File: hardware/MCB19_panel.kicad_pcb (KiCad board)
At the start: 2 copper layers, 204 x 171.5 mm, 218 parts, among them J401 USART, J402 DISABLE, J601 RJ45, J602 RJ45, J611 +BAT_IN, J612 -BAT_IN, J613 +BAT_OUT, J614 -BAT_OUT, Q601 IRFP260N, Q602 IRFP260N, U201 MCP2551-I/SN, U202 MCP2515-xSO, U301 LM7805, U401 ATMEGA328P-PU, U501 LM7815, U601 LM5104MNOPB, U602 INA240A4D, U603 LM324, Y201 16MHz, Y401 16MHz

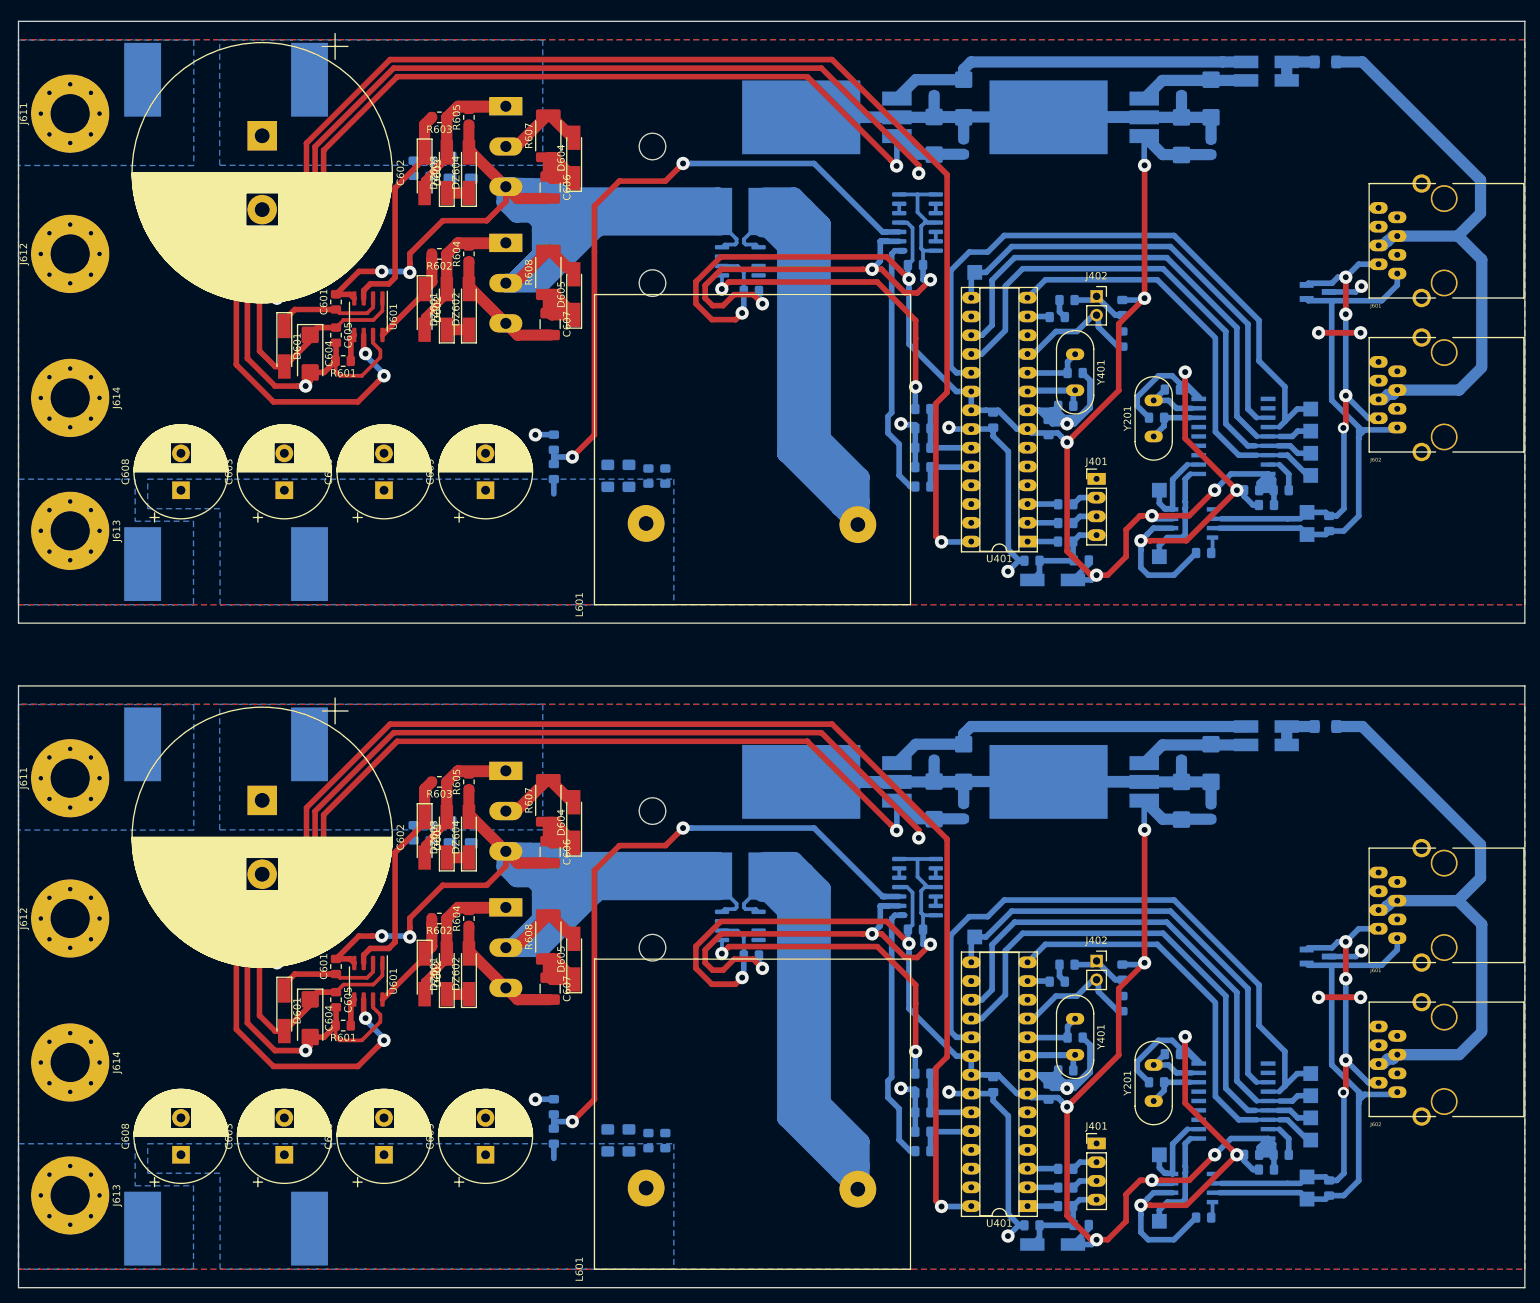
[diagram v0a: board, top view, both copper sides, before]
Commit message: small fixes in layout. Fabrication files exported.
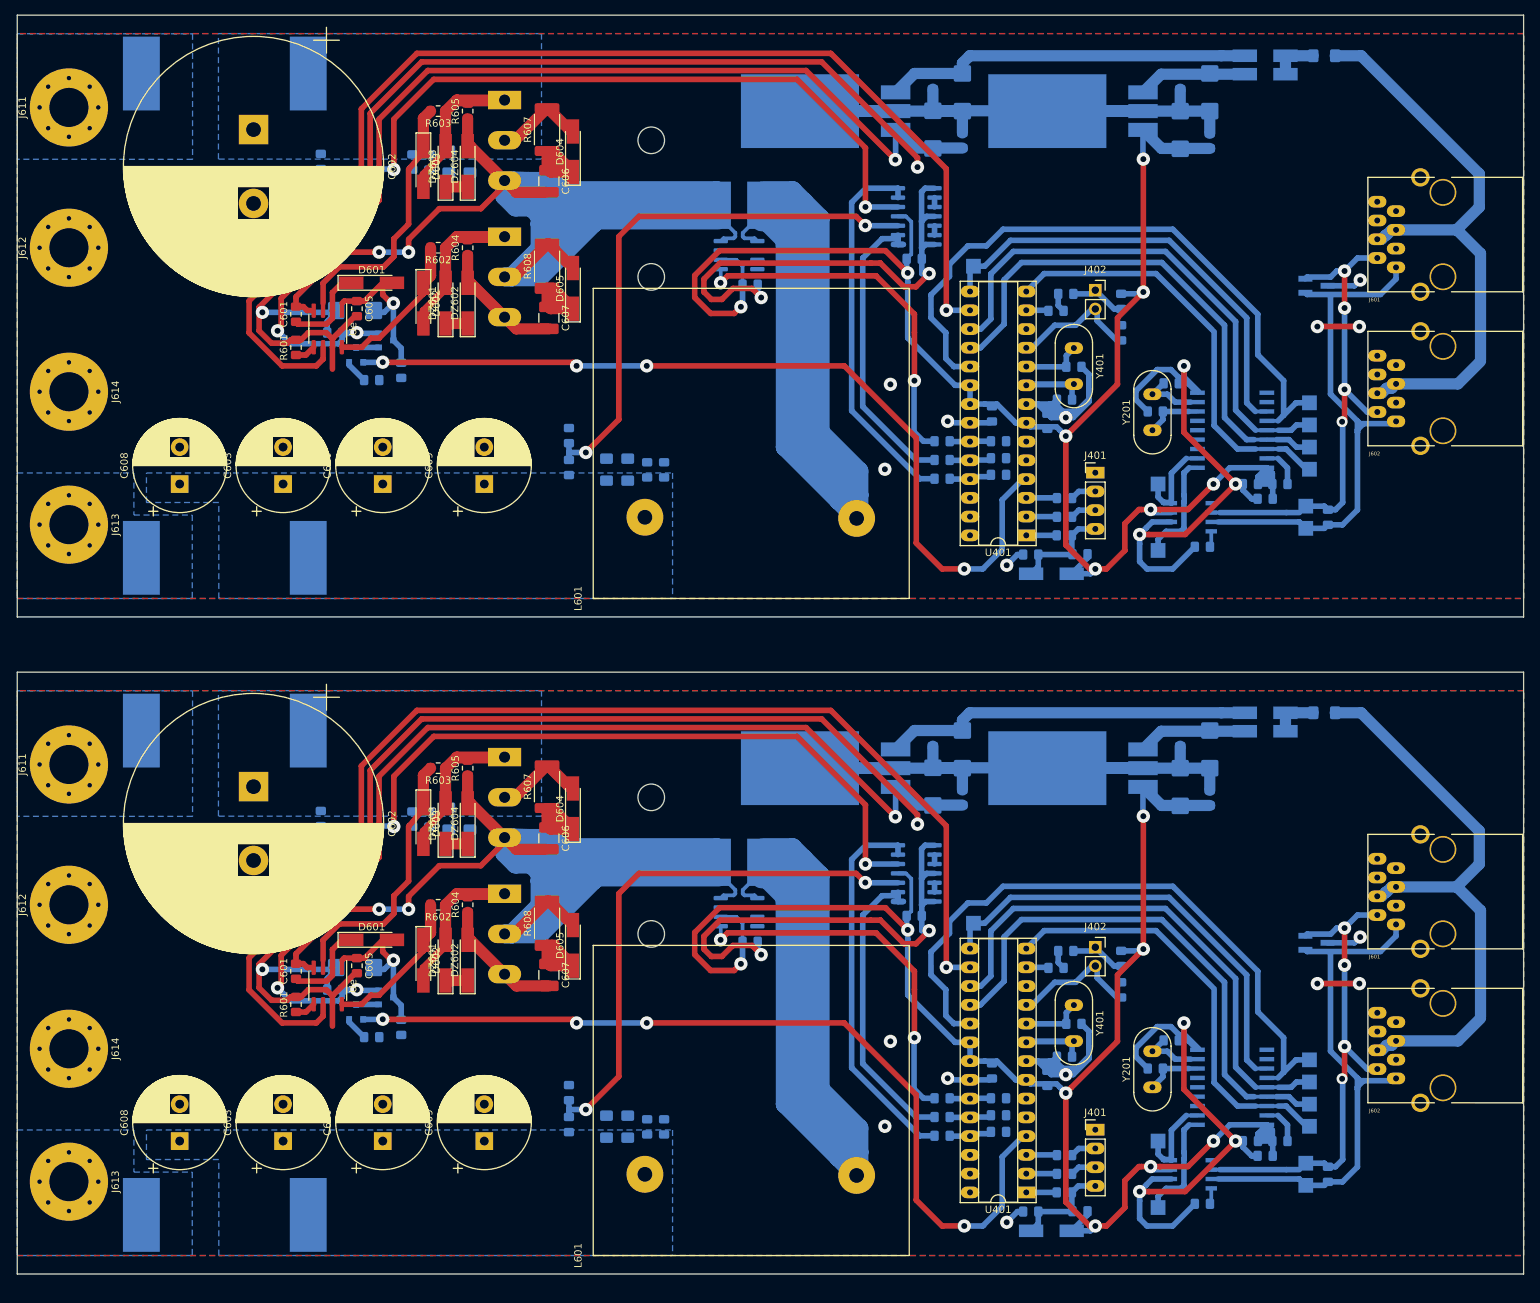
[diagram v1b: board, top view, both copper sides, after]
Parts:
- removed the D601 at (83.6, 154.9)
- removed the D601 at (83.6, 64.9)
- removed U601: LM5104MNOPB, Package_SO:SOIC-8_3.9x4.9mm_P1.27mm
- added C409: 100nF, Capacitor_SMD:C_0805_2012Metric_Pad1.15x1.40mm_HandSolder, B.Cu at (180.3, 171.2)
- added C409: 100nF, Capacitor_SMD:C_0805_2012Metric_Pad1.15x1.40mm_HandSolder, B.Cu at (180.3, 82.3)
- added C621: 100nF, Capacitor_SMD:C_0805_2012Metric_Pad1.15x1.40mm_HandSolder, B.Cu at (90.5, 152.0)
- added C621: 100nF, Capacitor_SMD:C_0805_2012Metric_Pad1.15x1.40mm_HandSolder, B.Cu at (90.5, 63.0)
- added D601: LL4148, Diode_SMD:D_MiniMELF_Handsoldering, F.Cu at (95.5, 145.2)
- added D601: LL4148, Diode_SMD:D_MiniMELF_Handsoldering, F.Cu at (95.5, 56.3)
- added Q603: BC857, Package_TO_SOT_SMD:SOT-23, B.Cu at (97.4, 153.0)
- added Q603: BC857, Package_TO_SOT_SMD:SOT-23, B.Cu at (97.4, 64.1)
- added Q604: BC847, Package_TO_SOT_SMD:SOT-23, B.Cu at (93.4, 155.0)
- added Q604: BC847, Package_TO_SOT_SMD:SOT-23, B.Cu at (93.4, 66.0)
- added R611: 1k, Resistor_SMD:R_0805_2012Metric_Pad1.15x1.40mm_HandSolder, B.Cu at (95.5, 158.4)
- added R611: 1k, Resistor_SMD:R_0805_2012Metric_Pad1.15x1.40mm_HandSolder, B.Cu at (95.5, 69.4)
- added R612: 1k, Resistor_SMD:R_0805_2012Metric_Pad1.15x1.40mm_HandSolder, B.Cu at (99.5, 157.1)
- added R612: 1k, Resistor_SMD:R_0805_2012Metric_Pad1.15x1.40mm_HandSolder, B.Cu at (99.5, 68.1)
- added R613: 15k, Resistor_SMD:R_0805_2012Metric_Pad1.15x1.40mm_HandSolder, B.Cu at (88.6, 128.8)
- added R613: 15k, Resistor_SMD:R_0805_2012Metric_Pad1.15x1.40mm_HandSolder, B.Cu at (88.6, 39.8)
- added R614: 1k2, Resistor_SMD:R_0805_2012Metric_Pad1.15x1.40mm_HandSolder, B.Cu at (88.6, 133.1)
- added R614: 1k2, Resistor_SMD:R_0805_2012Metric_Pad1.15x1.40mm_HandSolder, B.Cu at (88.6, 44.2)
- added Ue: LM5104MNOPB, Package_SO:SOIC-8_3.9x4.9mm_P1.27mm, F.Cu at (89.5, 151.5)
- C407 (x2): value 100n -> 100nF
- C604 (x2): moved to B.Cu
- R407 (x2), R408 (x2): value 1k5 -> 680
- R409 (x2): value 6k8 -> 680
- R609 (x2): value 470R -> 15k
- R610 (x2): value 1k5 -> 1k2
- moved C408 10.5 mm to (180.3, 169.0), turned to 0 degrees
- moved C407 10.4 mm to (180.3, 166.7), turned to 180 degrees
- moved C408 10.3 mm to (180.3, 80.0), turned to 0 degrees
- moved C407 10.3 mm to (180.3, 77.7), turned to 180 degrees
- moved C604 9.17 mm to (93.2, 149.0), turned to 180 degrees
- moved C604 8.43 mm to (93.2, 60.0), turned to 180 degrees
- moved R409 7.30 mm to (172.7, 82.8), turned to 180 degrees
- moved R601 7.01 mm to (85.2, 154.0), turned to 90 degrees
- moved R601 6.65 mm to (85.2, 65.0), turned to 90 degrees
- moved R409 6.36 mm to (172.7, 171.8), turned to 180 degrees
- moved R610 6.24 mm to (122.2, 165.9), turned to 270 degrees
- moved Ue 5.75 mm to (89.5, 62.5)
- moved C601 5.67 mm to (85.2, 60.5)
- moved C601 5.46 mm to (85.2, 149.5)
- moved C605 5.41 mm to (93.5, 148.8)
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- renumbered U601 to Ue
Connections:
- C604 pad 1: +15V -> Net-(C604-Pad1)
- C605 pad 1: +15V -> Net-(C604-Pad1)
- J601 pad 9: GND -> (no net)
- J602 pad 9: GND -> (no net)
- R409 pad 1: GND -> Net-(C409-Pad1)
- R409 pad 2: Net-(C407-Pad2) -> /driver/LM324B
- R609 pad 1: GND -> Net-(R609-Pad1)
- R609 pad 2: Net-(R609-Pad2) -> Net-(C603-Pad1)
- R610 pad 1: Net-(C603-Pad1) -> GND
- R610 pad 2: Net-(R609-Pad2) -> Net-(R609-Pad1)
- U401 pad 16: (no net) -> /MCU/PWM
- U401 pad 25: (no net) -> Net-(C409-Pad1)
- U401 pad 28: /MCU/PWM -> (no net)
- U401 pad 4: (no net) -> /MCU/ENABLE
- U603 pad 2: GND -> /driver/LM324A
- U603 pad 3: Net-(R609-Pad2) -> Net-(R609-Pad1)
- U603 pad 5: Net-(U603-Pad5) -> Net-(R613-Pad1)
- U603 pad 6: Net-(U603-Pad5) -> /driver/LM324B
- U603 pad 7: GND -> /driver/LM324B
- Ue pad 1: +15V -> Net-(C604-Pad1)
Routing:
- net (no net): track 2789.2 -> 2989.4 mm, vias 39 -> 44
- net /MCU/ENABLE: track 0.00 -> 119.1 mm, vias 0 -> 4
- net Net-(R613-Pad1): track 0.00 -> 101.3 mm, vias 0 -> 2
- net Net-(R609-Pad2): track 89.4 -> 0.00 mm, vias 2 -> 0
- net Net-(R609-Pad1): track 0.00 -> 75.1 mm, vias 0 -> 2
- net /MCU/PWM: track 217.1 -> 161.7 mm, vias 3 -> 1
- net /driver/LM324B: track 0.00 -> 51.6 mm
- net GND: track 558.8 -> 512.2 mm, vias 17 -> 15
- net Net-(C604-Pad1): track 0.00 -> 22.9 mm, vias 0 -> 1
- net +15V: track 158.4 -> 148.0 mm, vias 1 -> 3
- net /MCU/INALLL: track 42.7 -> 49.9 mm
- net Net-(D602-Pad1): track 13.7 -> 20.7 mm
- net Net-(D603-Pad1): track 30.3 -> 37.0 mm
- net Net-(C601-Pad2): track 253.7 -> 259.8 mm
- net Net-(Q603-Pad1): track 0.00 -> 6.12 mm
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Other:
- board size 204 x 171.5 mm -> 204 x 170.5 mm

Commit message: Some fixes, ready for heat transfering
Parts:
- removed the C201 at (197.0, 147.8)
- removed the C201 at (197.0, 58.8)
- removed the C202 at (214.5, 172.5)
- removed the C202 at (214.5, 83.5)
- removed the C203 at (201.6, 162.7)
- removed the C203 at (201.6, 73.7)
- removed the C204 at (203.7, 158.9)
- removed the C204 at (203.7, 69.9)
- removed the C205 at (216.5, 174.5)
- removed the C205 at (216.5, 85.5)
- removed the C301 at (209.0, 119.5)
- removed the C301 at (209.0, 30.5)
- removed the C302 at (205.0, 118.0)
- removed the C302 at (205.0, 29.0)
- removed the C303 at (209.0, 126.0)
- removed the C303 at (209.0, 37.0)
- removed the C304 at (205.0, 124.5)
- removed the C304 at (205.0, 35.6)
- removed the C401 at (187.0, 164.0)
- removed the C401 at (187.0, 75.0)
- removed the C402 at (179.5, 163.0)
- removed the C402 at (179.5, 74.0)
- removed the C403 at (190.6, 156.6)
- removed the C403 at (190.6, 67.6)
- removed the C404 at (189.3, 161.1)
- removed the C404 at (189.3, 72.1)
- removed the C406 at (184.7, 182.1)
- removed the C406 at (184.7, 93.1)
- removed the C407 at (180.3, 166.7)
- removed the C407 at (180.3, 77.7)
- removed the C408 at (180.3, 169.0)
- removed the C408 at (180.3, 80.0)
- removed the C409 at (180.3, 171.2)
- removed the C409 at (180.3, 82.3)
- removed the C501 at (175.5, 119.5)
- removed the C501 at (175.5, 30.5)
- removed the C502 at (171.5, 118.0)
- removed the C502 at (171.5, 29.0)
- removed the C503 at (175.5, 126.0)
- removed the C503 at (175.5, 37.0)
- removed the C504 at (171.5, 124.5)
- removed the C504 at (171.5, 35.5)
- removed the C601 at (85.2, 149.5)
- removed the C601 at (85.2, 60.5)
- removed the C602 at (79.5, 124.5)
- removed the C602 at (79.5, 35.5)
- removed the C603 at (83.5, 172.5)
- removed the C603 at (83.5, 83.5)
- removed the C604 at (93.2, 149.0)
- removed the C604 at (93.2, 60.0)
- removed the C605 at (93.5, 148.8)
- removed the C605 at (93.5, 59.8)
- removed the C606 at (119.5, 131.5)
- removed the C606 at (119.5, 42.5)
- removed the C607 at (119.5, 150.0)
- removed the C607 at (119.5, 61.0)
- removed the C608 at (69.5, 172.5)
- removed the C608 at (69.5, 83.5)
- removed the C609 at (110.7, 172.5)
- removed the C609 at (110.7, 83.5)
- removed the C610 at (97.0, 172.5)
- removed the C610 at (97.0, 83.5)
- removed the C611 at (146.7, 145.5)
- removed the C611 at (146.7, 56.5)
- removed the C612 at (168.9, 142.0)
- removed the C612 at (168.9, 53.0)
- removed the C613 at (108.8, 128.8)
- removed the C613 at (108.8, 39.9)
- removed the C614 at (105.9, 128.8)
- removed the C614 at (105.9, 39.9)
- removed the C615 at (101.0, 128.9)
- removed the C615 at (101.0, 39.9)
- removed the C616 at (103.3, 128.9)
- removed the C616 at (103.3, 39.9)
- removed the C617 at (130.1, 170.6)
- removed the C617 at (130.1, 81.6)
- removed the C618 at (127.3, 170.6)
- removed the C618 at (127.3, 81.6)
- removed the C619 at (135.1, 170.6)
- removed the C619 at (135.1, 81.6)
- removed the C620 at (132.8, 170.6)
- removed the C620 at (132.8, 81.6)
- removed the C621 at (90.5, 152.0)
- removed the C621 at (90.5, 63.0)
- removed the D201 at (223.4, 145.7)
- removed the D201 at (223.4, 56.7)
- removed the D301 at (216.5, 117.0)
- removed the D301 at (216.5, 28.0)
- removed the D401 at (187.5, 184.7)
- removed the D401 at (187.5, 95.7)
- removed the D403 at (189.5, 146.8)
- removed the D403 at (189.5, 57.8)
- removed the D501 at (216.5, 114.5)
- removed the D501 at (216.5, 25.5)
- removed the D601 at (95.5, 145.2)
- removed the D601 at (95.5, 56.3)
- removed the D602 at (102.5, 148.0)
- removed the D602 at (102.5, 59.0)
- removed the D603 at (102.5, 129.5)
- removed the D603 at (102.5, 40.5)
- removed the D604 at (122.7, 127.5)
- removed the D604 at (122.7, 38.5)
- removed the D605 at (122.7, 146.0)
- removed the D605 at (122.7, 57.0)
- removed the DZ601 at (105.5, 148.0)
- removed the DZ601 at (105.5, 59.0)
- removed the DZ602 at (108.5, 148.0)
- removed the DZ602 at (108.5, 59.0)
- removed the DZ603 at (105.5, 129.5)
- removed the DZ603 at (105.5, 40.5)
- removed the DZ604 at (108.5, 129.5)
- removed the DZ604 at (108.5, 40.5)
- removed the F501 at (224.5, 114.5)
- removed the F501 at (224.5, 25.5)
- removed the F601 at (86.9, 116.9)
- removed the F601 at (86.9, 27.9)
- removed the F602 at (64.3, 182.5)
- removed the F602 at (64.3, 93.5)
- removed the J401 at (193.5, 171.0)
- removed the J401 at (193.5, 82.0)
- removed the J402 at (193.5, 146.2)
- removed the J402 at (193.5, 57.3)
- removed the J601 at (234.2, 143.2)
- removed the J601 at (234.2, 54.2)
- removed the J602 at (234.2, 164.0)
- removed the J602 at (234.2, 75.0)
- removed the J611 at (54.5, 121.5)
- removed the J611 at (54.5, 32.5)
- removed the J612 at (54.5, 140.5)
- removed the J612 at (54.5, 51.5)
- removed the J613 at (54.5, 178.0)
- removed the J613 at (54.5, 89.0)
- removed the J614 at (54.5, 160.0)
- removed the J614 at (54.5, 71.0)
- removed the L601 at (125.5, 188.0)
- removed the L601 at (125.5, 99.0)
- removed the Q601 at (113.5, 120.5)
- removed the Q601 at (113.5, 31.5)
- removed the Q602 at (113.5, 139.0)
- removed the Q602 at (113.5, 50.0)
- removed the Q603 at (97.4, 153.0)
- removed the Q603 at (97.4, 64.1)
- removed the Q604 at (93.4, 155.0)
- removed the Q604 at (93.4, 66.0)
- removed the R201 at (225.0, 177.0)
- removed the R201 at (225.0, 88.0)
- removed the R202 at (208.0, 181.0)
- removed the R202 at (208.0, 92.0)
- removed the R203 at (218.5, 172.5)
- removed the R203 at (218.5, 83.5)
- removed the R401 at (191.4, 182.0)
- removed the R401 at (191.4, 93.0)
- removed the R402 at (189.3, 176.9)
- removed the R402 at (189.3, 88.0)
- removed the R403 at (189.3, 174.4)
- removed the R403 at (189.3, 85.4)
- removed the R406 at (188.1, 149.1)
- removed the R406 at (188.1, 60.1)
- removed the R407 at (172.7, 166.7)
- removed the R407 at (172.7, 77.7)
- removed the R408 at (172.7, 169.2)
- removed the R408 at (172.7, 80.3)
- removed the R409 at (172.7, 171.8)
- removed the R409 at (172.7, 82.8)
- removed the R410 at (197.0, 152.0)
- removed the R410 at (197.0, 63.0)
- removed the R411 at (189.3, 179.4)
- removed the R411 at (189.3, 90.5)
- removed the R601 at (85.2, 154.0)
- removed the R601 at (85.2, 65.0)
- removed the R602 at (104.5, 140.5)
- removed the R602 at (104.5, 51.5)
- removed the R603 at (104.5, 122.0)
- removed the R603 at (104.5, 33.0)
- removed the R604 at (108.5, 140.5)
- removed the R604 at (108.5, 51.5)
- removed the R605 at (108.5, 122.0)
- removed the R605 at (108.5, 33.0)
- removed the R606 at (145.2, 134.8)
- removed the R606 at (145.2, 45.8)
- removed the R607 at (119.2, 124.5)
- removed the R607 at (119.2, 35.5)
- removed the R608 at (119.2, 143.0)
- removed the R608 at (119.2, 54.0)
- removed the R609 at (122.2, 170.3)
- removed the R609 at (122.2, 81.3)
- removed the R610 at (122.2, 165.9)
- removed the R610 at (122.2, 77.0)
- removed the R611 at (95.5, 158.4)
- removed the R611 at (95.5, 69.4)
- removed the R612 at (99.5, 157.1)
- removed the R612 at (99.5, 68.1)
- removed the R613 at (88.6, 128.8)
- removed the R613 at (88.6, 39.8)
- removed the R614 at (88.6, 133.1)
- removed the R614 at (88.6, 44.2)
- removed the TP201 at (222.5, 164.5)
- removed the TP201 at (222.5, 75.5)
- removed the TP202 at (222.5, 167.5)
- removed the TP202 at (222.5, 78.5)
- removed the TP203 at (202.0, 181.5)
- removed the TP203 at (202.0, 92.5)
- removed the TP204 at (202.0, 172.5)
- removed the TP204 at (202.0, 83.5)
- removed the TP205 at (222.5, 170.5)
- removed the TP205 at (222.5, 81.5)
- removed the TP206 at (222.5, 161.5)
- removed the TP206 at (222.5, 72.5)
- removed the TP207 at (222.0, 178.5)
- removed the TP207 at (222.0, 89.5)
- removed the TP208 at (222.0, 175.5)
- removed the TP208 at (222.0, 86.5)
- removed the TP209 at (177.0, 143.0)
- removed the TP209 at (177.0, 54.0)
- removed the U201 at (206.5, 177.0)
- removed the U201 at (206.5, 88.0)
- removed the U202 at (212.0, 165.2)
- removed the U202 at (212.0, 76.2)
- removed the U301 at (198.6, 119.5)
- removed the U301 at (198.6, 30.5)
- removed the U401 at (184.1, 179.4)
- removed the U401 at (184.1, 90.5)
- removed the U501 at (165.1, 119.5)
- removed the U501 at (165.1, 30.5)
- removed the U602 at (145.2, 141.5)
- removed the U602 at (145.2, 52.5)
- removed the U603 at (169.2, 136.2)
- removed the U603 at (169.2, 47.3)
- removed Ue (x2): LM5104MNOPB, Package_SO:SOIC-8_3.9x4.9mm_P1.27mm
- removed the Y201 at (201.2, 165.2)
- removed the Y201 at (201.2, 76.2)
- removed the Y401 at (190.6, 154.1)
- removed the Y401 at (190.6, 65.1)
- added C201: 100nF, Capacitor_SMD:C_0805_2012Metric_Pad1.15x1.40mm_HandSolder, B.Cu at (236.5, 69.1)
- added C201: 100nF, Capacitor_SMD:C_0805_2012Metric_Pad1.15x1.40mm_HandSolder, B.Cu at (146.5, 69.1)
- added C201: 100nF, Capacitor_SMD:C_0805_2012Metric_Pad1.15x1.40mm_HandSolder, B.Cu at (56.5, 69.1)
- added C202: 100nF, Capacitor_SMD:C_0805_2012Metric_Pad1.15x1.40mm_HandSolder, B.Cu at (261.2, 51.6)
- added C202: 100nF, Capacitor_SMD:C_0805_2012Metric_Pad1.15x1.40mm_HandSolder, B.Cu at (171.2, 51.6)
- added C202: 100nF, Capacitor_SMD:C_0805_2012Metric_Pad1.15x1.40mm_HandSolder, B.Cu at (81.2, 51.6)
- added C203: 22pF, Capacitor_SMD:C_0805_2012Metric_Pad1.15x1.40mm_HandSolder, B.Cu at (251.4, 64.5)
- added C203: 22pF, Capacitor_SMD:C_0805_2012Metric_Pad1.15x1.40mm_HandSolder, B.Cu at (161.4, 64.5)
- added C203: 22pF, Capacitor_SMD:C_0805_2012Metric_Pad1.15x1.40mm_HandSolder, B.Cu at (71.4, 64.5)
- added C204: 22pF, Capacitor_SMD:C_0805_2012Metric_Pad1.15x1.40mm_HandSolder, B.Cu at (247.6, 62.3)
- added C204: 22pF, Capacitor_SMD:C_0805_2012Metric_Pad1.15x1.40mm_HandSolder, B.Cu at (157.6, 62.3)
- added C204: 22pF, Capacitor_SMD:C_0805_2012Metric_Pad1.15x1.40mm_HandSolder, B.Cu at (67.6, 62.3)
- added C205: 100nF, Capacitor_SMD:C_0805_2012Metric_Pad1.15x1.40mm_HandSolder, B.Cu at (263.2, 49.6)
- added C205: 100nF, Capacitor_SMD:C_0805_2012Metric_Pad1.15x1.40mm_HandSolder, B.Cu at (173.2, 49.6)
- added C205: 100nF, Capacitor_SMD:C_0805_2012Metric_Pad1.15x1.40mm_HandSolder, B.Cu at (83.2, 49.6)
- added C301: 1uF, Capacitor_Tantalum_SMD:CP_EIA-6032-20_AVX-F_Pad2.25x2.35mm_HandSolder, B.Cu at (208.8, 31.9)
- added C301: 1uF, Capacitor_Tantalum_SMD:CP_EIA-6032-20_AVX-F_Pad2.25x2.35mm_HandSolder, B.Cu at (118.8, 31.9)
- added C301: 1uF, Capacitor_Tantalum_SMD:CP_EIA-6032-20_AVX-F_Pad2.25x2.35mm_HandSolder, B.Cu at (28.8, 31.9)
- added C302: 100nF, Capacitor_SMD:C_0805_2012Metric_Pad1.15x1.40mm_HandSolder, B.Cu at (207.3, 35.9)
- added C302: 100nF, Capacitor_SMD:C_0805_2012Metric_Pad1.15x1.40mm_HandSolder, B.Cu at (117.3, 35.9)
- added C302: 100nF, Capacitor_SMD:C_0805_2012Metric_Pad1.15x1.40mm_HandSolder, B.Cu at (27.3, 35.9)
- added C303: 100nF, Capacitor_SMD:C_0805_2012Metric_Pad1.15x1.40mm_HandSolder, B.Cu at (215.3, 31.9)
- added C303: 100nF, Capacitor_SMD:C_0805_2012Metric_Pad1.15x1.40mm_HandSolder, B.Cu at (125.3, 31.9)
- added C303: 100nF, Capacitor_SMD:C_0805_2012Metric_Pad1.15x1.40mm_HandSolder, B.Cu at (35.3, 31.9)
- added C304: 1uF, Capacitor_Tantalum_SMD:CP_EIA-6032-20_AVX-F_Pad2.25x2.35mm_HandSolder, B.Cu at (213.8, 35.9)
- added C304: 1uF, Capacitor_Tantalum_SMD:CP_EIA-6032-20_AVX-F_Pad2.25x2.35mm_HandSolder, B.Cu at (123.8, 35.9)
- added C304: 1uF, Capacitor_Tantalum_SMD:CP_EIA-6032-20_AVX-F_Pad2.25x2.35mm_HandSolder, B.Cu at (33.9, 35.9)
- added C401: 100nF, Capacitor_SMD:C_0805_2012Metric_Pad1.15x1.40mm_HandSolder, B.Cu at (252.7, 79.1)
- added C401: 100nF, Capacitor_SMD:C_0805_2012Metric_Pad1.15x1.40mm_HandSolder, B.Cu at (162.7, 79.1)
- added C401: 100nF, Capacitor_SMD:C_0805_2012Metric_Pad1.15x1.40mm_HandSolder, B.Cu at (72.7, 79.1)
- added C402: 100nF, Capacitor_SMD:C_0805_2012Metric_Pad1.15x1.40mm_HandSolder, B.Cu at (251.7, 86.6)
- added C402: 100nF, Capacitor_SMD:C_0805_2012Metric_Pad1.15x1.40mm_HandSolder, B.Cu at (161.7, 86.6)
- added C402: 100nF, Capacitor_SMD:C_0805_2012Metric_Pad1.15x1.40mm_HandSolder, B.Cu at (71.7, 86.6)
- added C403: 22pF, Capacitor_SMD:C_0805_2012Metric_Pad1.15x1.40mm_HandSolder, B.Cu at (245.3, 75.5)
- added C403: 22pF, Capacitor_SMD:C_0805_2012Metric_Pad1.15x1.40mm_HandSolder, B.Cu at (155.3, 75.5)
- added C403: 22pF, Capacitor_SMD:C_0805_2012Metric_Pad1.15x1.40mm_HandSolder, B.Cu at (65.3, 75.5)
- added C404: 22pF, Capacitor_SMD:C_0805_2012Metric_Pad1.15x1.40mm_HandSolder, B.Cu at (249.8, 76.8)
- added C404: 22pF, Capacitor_SMD:C_0805_2012Metric_Pad1.15x1.40mm_HandSolder, B.Cu at (159.8, 76.8)
- added C404: 22pF, Capacitor_SMD:C_0805_2012Metric_Pad1.15x1.40mm_HandSolder, B.Cu at (69.8, 76.8)
- added C406: 100nF, Capacitor_SMD:C_0805_2012Metric_Pad1.15x1.40mm_HandSolder, B.Cu at (270.8, 81.3)
- added C406: 100nF, Capacitor_SMD:C_0805_2012Metric_Pad1.15x1.40mm_HandSolder, B.Cu at (180.8, 81.3)
- added C406: 100nF, Capacitor_SMD:C_0805_2012Metric_Pad1.15x1.40mm_HandSolder, B.Cu at (90.8, 81.3)
- added C407: 100nF, Capacitor_SMD:C_0805_2012Metric_Pad1.15x1.40mm_HandSolder, B.Cu at (255.4, 85.7)
- added C407: 100nF, Capacitor_SMD:C_0805_2012Metric_Pad1.15x1.40mm_HandSolder, B.Cu at (165.4, 85.7)
- added C407: 100nF, Capacitor_SMD:C_0805_2012Metric_Pad1.15x1.40mm_HandSolder, B.Cu at (75.4, 85.7)
- added C408: 100nF, Capacitor_SMD:C_0805_2012Metric_Pad1.15x1.40mm_HandSolder, B.Cu at (257.7, 85.7)
- added C408: 100nF, Capacitor_SMD:C_0805_2012Metric_Pad1.15x1.40mm_HandSolder, B.Cu at (167.7, 85.7)
- added C408: 100nF, Capacitor_SMD:C_0805_2012Metric_Pad1.15x1.40mm_HandSolder, B.Cu at (77.7, 85.7)
- added C409: 100nF, Capacitor_SMD:C_0805_2012Metric_Pad1.15x1.40mm_HandSolder, B.Cu at (259.9, 85.7)
- added C409: 100nF, Capacitor_SMD:C_0805_2012Metric_Pad1.15x1.40mm_HandSolder, B.Cu at (169.9, 85.7)
- added C409: 100nF, Capacitor_SMD:C_0805_2012Metric_Pad1.15x1.40mm_HandSolder, B.Cu at (80.0, 85.7)
- added C501: 1uF, Capacitor_Tantalum_SMD:CP_EIA-6032-20_AVX-F_Pad2.25x2.35mm_HandSolder, B.Cu at (208.8, 65.4)
- added C501: 1uF, Capacitor_Tantalum_SMD:CP_EIA-6032-20_AVX-F_Pad2.25x2.35mm_HandSolder, B.Cu at (118.8, 65.4)
- added C501: 1uF, Capacitor_Tantalum_SMD:CP_EIA-6032-20_AVX-F_Pad2.25x2.35mm_HandSolder, B.Cu at (28.8, 65.4)
- added C502: 100nF, Capacitor_SMD:C_0805_2012Metric_Pad1.15x1.40mm_HandSolder, B.Cu at (207.3, 69.4)
- added C502: 100nF, Capacitor_SMD:C_0805_2012Metric_Pad1.15x1.40mm_HandSolder, B.Cu at (117.3, 69.4)
- added C502: 100nF, Capacitor_SMD:C_0805_2012Metric_Pad1.15x1.40mm_HandSolder, B.Cu at (27.3, 69.4)
- added C503: 100nF, Capacitor_SMD:C_0805_2012Metric_Pad1.15x1.40mm_HandSolder, B.Cu at (215.3, 65.4)
- added C503: 100nF, Capacitor_SMD:C_0805_2012Metric_Pad1.15x1.40mm_HandSolder, B.Cu at (125.3, 65.4)
- added C503: 100nF, Capacitor_SMD:C_0805_2012Metric_Pad1.15x1.40mm_HandSolder, B.Cu at (35.3, 65.4)
- added C504: 1uF, Capacitor_Tantalum_SMD:CP_EIA-6032-20_AVX-F_Pad2.25x2.35mm_HandSolder, B.Cu at (213.8, 69.4)
- added C504: 1uF, Capacitor_Tantalum_SMD:CP_EIA-6032-20_AVX-F_Pad2.25x2.35mm_HandSolder, B.Cu at (123.8, 69.4)
- added C504: 1uF, Capacitor_Tantalum_SMD:CP_EIA-6032-20_AVX-F_Pad2.25x2.35mm_HandSolder, B.Cu at (33.8, 69.4)
- added C601: 100nF, Capacitor_SMD:C_0805_2012Metric_Pad1.15x1.40mm_HandSolder, B.Cu at (231.4, 130.1)
- added C601: 100nF, Capacitor_SMD:C_0805_2012Metric_Pad1.15x1.40mm_HandSolder, B.Cu at (141.4, 130.1)
- added C601: 100nF, Capacitor_SMD:C_0805_2012Metric_Pad1.15x1.40mm_HandSolder, B.Cu at (51.4, 130.1)
- added C602: 4700uF, Capacitor_THT:CP_Radial_D12.5mm_P5.00mm, F.Cu at (214.7, 168.5)
- added C602: 4700uF, Capacitor_THT:CP_Radial_D12.5mm_P5.00mm, F.Cu at (124.7, 168.5)
- added C602: 4700uF, Capacitor_THT:CP_Radial_D12.5mm_P5.00mm, F.Cu at (34.6, 168.5)
- added C603: 47uF, Capacitor_THT:CP_Radial_D12.5mm_P5.00mm, F.Cu at (230.4, 157.7)
- added C603: 47uF, Capacitor_THT:CP_Radial_D12.5mm_P5.00mm, F.Cu at (140.4, 157.7)
- added C603: 47uF, Capacitor_THT:CP_Radial_D12.5mm_P5.00mm, F.Cu at (50.4, 157.7)
- added C604: 1uF, Capacitor_Tantalum_SMD:CP_EIA-6032-20_AVX-F_Pad2.25x2.35mm_HandSolder, B.Cu at (224.8, 138.4)
- added C604: 1uF, Capacitor_Tantalum_SMD:CP_EIA-6032-20_AVX-F_Pad2.25x2.35mm_HandSolder, B.Cu at (134.8, 138.4)
- added C604: 1uF, Capacitor_Tantalum_SMD:CP_EIA-6032-20_AVX-F_Pad2.25x2.35mm_HandSolder, B.Cu at (44.8, 138.4)
- added C605: 100nF, Capacitor_SMD:C_0805_2012Metric_Pad1.15x1.40mm_HandSolder, B.Cu at (229.5, 140.5)
- added C605: 100nF, Capacitor_SMD:C_0805_2012Metric_Pad1.15x1.40mm_HandSolder, B.Cu at (139.5, 140.5)
- added C605: 100nF, Capacitor_SMD:C_0805_2012Metric_Pad1.15x1.40mm_HandSolder, B.Cu at (49.5, 140.5)
- added C606: 47nF, Capacitor_SMD:C_1210_3225Metric_Pad1.42x2.65mm_HandSolder, F.Cu at (220.0, 118.5)
- added C606: 47nF, Capacitor_SMD:C_1210_3225Metric_Pad1.42x2.65mm_HandSolder, F.Cu at (130.0, 118.5)
- added C606: 47nF, Capacitor_SMD:C_1210_3225Metric_Pad1.42x2.65mm_HandSolder, F.Cu at (40.0, 118.5)
- added C607: 47nF, Capacitor_SMD:C_1210_3225Metric_Pad1.42x2.65mm_HandSolder, F.Cu at (238.5, 118.5)
- added C607: 47nF, Capacitor_SMD:C_1210_3225Metric_Pad1.42x2.65mm_HandSolder, F.Cu at (148.5, 118.5)
- added C607: 47nF, Capacitor_SMD:C_1210_3225Metric_Pad1.42x2.65mm_HandSolder, F.Cu at (58.5, 118.5)
- added C608: 47uF, Capacitor_THT:CP_Radial_D12.5mm_P5.00mm, F.Cu at (243.6, 157.7)
- added C608: 47uF, Capacitor_THT:CP_Radial_D12.5mm_P5.00mm, F.Cu at (153.6, 157.7)
- added C608: 47uF, Capacitor_THT:CP_Radial_D12.5mm_P5.00mm, F.Cu at (63.5, 157.7)
- added C609: 47uF, Capacitor_THT:CP_Radial_D12.5mm_P5.00mm, F.Cu at (243.6, 166.1)
- added C609: 47uF, Capacitor_THT:CP_Radial_D12.5mm_P5.00mm, F.Cu at (153.6, 166.1)
- added C609: 47uF, Capacitor_THT:CP_Radial_D12.5mm_P5.00mm, F.Cu at (63.5, 166.1)
- added C610: 47uF, Capacitor_THT:CP_Radial_D12.5mm_P5.00mm, F.Cu at (230.4, 166.1)
- added C610: 47uF, Capacitor_THT:CP_Radial_D12.5mm_P5.00mm, F.Cu at (140.4, 166.1)
- added C610: 47uF, Capacitor_THT:CP_Radial_D12.5mm_P5.00mm, F.Cu at (50.4, 166.1)
- added C611: 100nF, Capacitor_SMD:C_0805_2012Metric_Pad1.15x1.40mm_HandSolder, B.Cu at (247.4, 128.3)
- added C611: 100nF, Capacitor_SMD:C_0805_2012Metric_Pad1.15x1.40mm_HandSolder, B.Cu at (157.4, 128.3)
- added C611: 100nF, Capacitor_SMD:C_0805_2012Metric_Pad1.15x1.40mm_HandSolder, B.Cu at (67.5, 128.3)
- added C612: 100nF, Capacitor_SMD:C_0805_2012Metric_Pad1.15x1.40mm_HandSolder, B.Cu at (266.9, 102.7)
- added C612: 100nF, Capacitor_SMD:C_0805_2012Metric_Pad1.15x1.40mm_HandSolder, B.Cu at (176.9, 102.7)
- added C612: 100nF, Capacitor_SMD:C_0805_2012Metric_Pad1.15x1.40mm_HandSolder, B.Cu at (87.0, 102.7)
- added C613: 4.7u, Capacitor_SMD:C_1206_3216Metric_Pad1.42x1.75mm_HandSolder, F.Cu at (216.9, 111.1)
- added C613: 4.7u, Capacitor_SMD:C_1206_3216Metric_Pad1.42x1.75mm_HandSolder, F.Cu at (126.9, 111.1)
- added C613: 4.7u, Capacitor_SMD:C_1206_3216Metric_Pad1.42x1.75mm_HandSolder, F.Cu at (36.9, 111.1)
- added C614: 4.7u, Capacitor_SMD:C_1206_3216Metric_Pad1.42x1.75mm_HandSolder, F.Cu at (214.0, 111.1)
- added C614: 4.7u, Capacitor_SMD:C_1206_3216Metric_Pad1.42x1.75mm_HandSolder, F.Cu at (124.0, 111.1)
- added C614: 4.7u, Capacitor_SMD:C_1206_3216Metric_Pad1.42x1.75mm_HandSolder, F.Cu at (34.0, 111.1)
- added C615: 100n, Capacitor_SMD:C_0805_2012Metric_Pad1.15x1.40mm_HandSolder, F.Cu at (219.5, 111.6)
- added C615: 100n, Capacitor_SMD:C_0805_2012Metric_Pad1.15x1.40mm_HandSolder, F.Cu at (129.5, 111.6)
- added C615: 100n, Capacitor_SMD:C_0805_2012Metric_Pad1.15x1.40mm_HandSolder, F.Cu at (39.5, 111.6)
- added C616: 100n, Capacitor_SMD:C_0805_2012Metric_Pad1.15x1.40mm_HandSolder, F.Cu at (221.8, 111.6)
- added C616: 100n, Capacitor_SMD:C_0805_2012Metric_Pad1.15x1.40mm_HandSolder, F.Cu at (131.8, 111.6)
- added C616: 100n, Capacitor_SMD:C_0805_2012Metric_Pad1.15x1.40mm_HandSolder, F.Cu at (41.8, 111.6)
- added C617: 4.7u, Capacitor_SMD:C_1206_3216Metric_Pad1.42x1.75mm_HandSolder, B.Cu at (235.9, 156.0)
- added C617: 4.7u, Capacitor_SMD:C_1206_3216Metric_Pad1.42x1.75mm_HandSolder, B.Cu at (145.9, 156.0)
- added C617: 4.7u, Capacitor_SMD:C_1206_3216Metric_Pad1.42x1.75mm_HandSolder, B.Cu at (55.9, 156.0)
- added C618: 4.7u, Capacitor_SMD:C_1206_3216Metric_Pad1.42x1.75mm_HandSolder, B.Cu at (233.0, 156.0)
- added C618: 4.7u, Capacitor_SMD:C_1206_3216Metric_Pad1.42x1.75mm_HandSolder, B.Cu at (143.0, 156.0)
- added C618: 4.7u, Capacitor_SMD:C_1206_3216Metric_Pad1.42x1.75mm_HandSolder, B.Cu at (53.0, 156.0)
- added C619: 100n, Capacitor_SMD:C_0805_2012Metric_Pad1.15x1.40mm_HandSolder, B.Cu at (240.8, 156.0)
- added C619: 100n, Capacitor_SMD:C_0805_2012Metric_Pad1.15x1.40mm_HandSolder, B.Cu at (150.8, 156.0)
- added C619: 100n, Capacitor_SMD:C_0805_2012Metric_Pad1.15x1.40mm_HandSolder, B.Cu at (60.8, 156.0)
- added C620: 100n, Capacitor_SMD:C_0805_2012Metric_Pad1.15x1.40mm_HandSolder, B.Cu at (238.5, 156.0)
- added C620: 100n, Capacitor_SMD:C_0805_2012Metric_Pad1.15x1.40mm_HandSolder, B.Cu at (148.5, 156.0)
- added C620: 100n, Capacitor_SMD:C_0805_2012Metric_Pad1.15x1.40mm_HandSolder, B.Cu at (58.5, 156.0)
- added C621: 4700uF, Capacitor_THT:CP_Radial_D12.5mm_P5.00mm, F.Cu at (214.7, 155.1)
- added C621: 4700uF, Capacitor_THT:CP_Radial_D12.5mm_P5.00mm, F.Cu at (124.7, 155.1)
- added C621: 4700uF, Capacitor_THT:CP_Radial_D12.5mm_P5.00mm, F.Cu at (34.6, 155.1)
- added C622: 100n, Capacitor_SMD:C_0805_2012Metric_Pad1.15x1.40mm_HandSolder, F.Cu at (226.6, 111.5)
- added C622: 100n, Capacitor_SMD:C_0805_2012Metric_Pad1.15x1.40mm_HandSolder, F.Cu at (136.6, 111.5)
- added C622: 100n, Capacitor_SMD:C_0805_2012Metric_Pad1.15x1.40mm_HandSolder, F.Cu at (46.6, 111.5)
- added C623: 100n, Capacitor_SMD:C_0805_2012Metric_Pad1.15x1.40mm_HandSolder, F.Cu at (224.2, 111.5)
- added C623: 100n, Capacitor_SMD:C_0805_2012Metric_Pad1.15x1.40mm_HandSolder, F.Cu at (134.2, 111.5)
- added C623: 100n, Capacitor_SMD:C_0805_2012Metric_Pad1.15x1.40mm_HandSolder, F.Cu at (44.2, 111.5)
- added C624: 100n, Capacitor_SMD:C_0805_2012Metric_Pad1.15x1.40mm_HandSolder, F.Cu at (229.0, 111.5)
- added C624: 100n, Capacitor_SMD:C_0805_2012Metric_Pad1.15x1.40mm_HandSolder, F.Cu at (139.0, 111.5)
- added C624: 100n, Capacitor_SMD:C_0805_2012Metric_Pad1.15x1.40mm_HandSolder, F.Cu at (49.0, 111.5)
- added C625: 100n, Capacitor_SMD:C_0805_2012Metric_Pad1.15x1.40mm_HandSolder, F.Cu at (231.4, 111.5)
- added C625: 100n, Capacitor_SMD:C_0805_2012Metric_Pad1.15x1.40mm_HandSolder, F.Cu at (141.4, 111.5)
- added C625: 100n, Capacitor_SMD:C_0805_2012Metric_Pad1.15x1.40mm_HandSolder, F.Cu at (51.4, 111.5)
- added C626: 100n, Capacitor_SMD:C_0805_2012Metric_Pad1.15x1.40mm_HandSolder, F.Cu at (233.8, 111.5)
- added C626: 100n, Capacitor_SMD:C_0805_2012Metric_Pad1.15x1.40mm_HandSolder, F.Cu at (143.8, 111.5)
- added C626: 100n, Capacitor_SMD:C_0805_2012Metric_Pad1.15x1.40mm_HandSolder, F.Cu at (53.8, 111.5)
- added C627: 100n, Capacitor_SMD:C_0805_2012Metric_Pad1.15x1.40mm_HandSolder, F.Cu at (236.2, 111.5)
- added C627: 100n, Capacitor_SMD:C_0805_2012Metric_Pad1.15x1.40mm_HandSolder, F.Cu at (146.2, 111.5)
- added C627: 100n, Capacitor_SMD:C_0805_2012Metric_Pad1.15x1.40mm_HandSolder, F.Cu at (56.2, 111.5)
- added C628: 1uF, Capacitor_Tantalum_SMD:CP_EIA-6032-20_AVX-F_Pad2.25x2.35mm_HandSolder, B.Cu at (271.2, 138.5)
- added C628: 1uF, Capacitor_Tantalum_SMD:CP_EIA-6032-20_AVX-F_Pad2.25x2.35mm_HandSolder, B.Cu at (181.2, 138.5)
- added C628: 1uF, Capacitor_Tantalum_SMD:CP_EIA-6032-20_AVX-F_Pad2.25x2.35mm_HandSolder, B.Cu at (91.2, 138.5)
- added C629: 100nF, Capacitor_SMD:C_0805_2012Metric_Pad1.15x1.40mm_HandSolder, B.Cu at (267.6, 141.1)
- added C629: 100nF, Capacitor_SMD:C_0805_2012Metric_Pad1.15x1.40mm_HandSolder, B.Cu at (177.6, 141.1)
- added C629: 100nF, Capacitor_SMD:C_0805_2012Metric_Pad1.15x1.40mm_HandSolder, B.Cu at (87.6, 141.1)
- added D201: pesd1can, Package_TO_SOT_SMD:SOT-23_Handsoldering, B.Cu at (234.3, 42.6)
- added D201: pesd1can, Package_TO_SOT_SMD:SOT-23_Handsoldering, B.Cu at (144.3, 42.6)
- added D201: pesd1can, Package_TO_SOT_SMD:SOT-23_Handsoldering, B.Cu at (54.4, 42.6)
- added D301: LL4148, Diode_SMD:D_MiniMELF_Handsoldering, B.Cu at (206.3, 24.4)
- added D301: LL4148, Diode_SMD:D_MiniMELF_Handsoldering, B.Cu at (116.3, 24.4)
- added D301: LL4148, Diode_SMD:D_MiniMELF_Handsoldering, B.Cu at (26.3, 24.4)
- added D401: LL4148, Diode_SMD:D_MiniMELF_Handsoldering, B.Cu at (273.4, 77.6)
- added D401: LL4148, Diode_SMD:D_MiniMELF_Handsoldering, B.Cu at (183.4, 77.6)
- added D401: LL4148, Diode_SMD:D_MiniMELF_Handsoldering, B.Cu at (93.4, 77.6)
- added D402: LED_RED, LED_SMD:LED_0805_2012Metric_Pad1.15x1.40mm_HandSolder, B.Cu at (260.0, 76.9)
- added D402: LED_RED, LED_SMD:LED_0805_2012Metric_Pad1.15x1.40mm_HandSolder, B.Cu at (170.0, 76.9)
- added D402: LED_RED, LED_SMD:LED_0805_2012Metric_Pad1.15x1.40mm_HandSolder, B.Cu at (80.0, 76.9)
- added D403: LED_RED, LED_SMD:LED_0805_2012Metric_Pad1.15x1.40mm_HandSolder, B.Cu at (235.4, 76.6)
- added D403: LED_RED, LED_SMD:LED_0805_2012Metric_Pad1.15x1.40mm_HandSolder, B.Cu at (145.4, 76.6)
- added D403: LED_RED, LED_SMD:LED_0805_2012Metric_Pad1.15x1.40mm_HandSolder, B.Cu at (55.5, 76.6)
- added D501: LL4148, Diode_SMD:D_MiniMELF_Handsoldering, B.Cu at (203.8, 24.4)
- added D501: LL4148, Diode_SMD:D_MiniMELF_Handsoldering, B.Cu at (113.8, 24.4)
- added D501: LL4148, Diode_SMD:D_MiniMELF_Handsoldering, B.Cu at (23.8, 24.4)
- added D601: LL4148, Diode_SMD:D_MiniMELF_Handsoldering, B.Cu at (227.9, 133.6)
- added D601: LL4148, Diode_SMD:D_MiniMELF_Handsoldering, B.Cu at (137.9, 133.6)
- added D601: LL4148, Diode_SMD:D_MiniMELF_Handsoldering, B.Cu at (47.9, 133.6)
- added D602: LL4148, Diode_SMD:D_MiniMELF_Handsoldering, F.Cu at (236.5, 135.5)
- added D602: LL4148, Diode_SMD:D_MiniMELF_Handsoldering, F.Cu at (146.5, 135.5)
- added D602: LL4148, Diode_SMD:D_MiniMELF_Handsoldering, F.Cu at (56.5, 135.5)
- added D603: LL4148, Diode_SMD:D_MiniMELF_Handsoldering, F.Cu at (218.0, 135.5)
- added D603: LL4148, Diode_SMD:D_MiniMELF_Handsoldering, F.Cu at (128.0, 135.5)
- added D603: LL4148, Diode_SMD:D_MiniMELF_Handsoldering, F.Cu at (38.0, 135.5)
- added D604: ES2A, Diode_SMD:D_MiniMELF_Handsoldering, F.Cu at (216.0, 115.2)
- added D604: ES2A, Diode_SMD:D_MiniMELF_Handsoldering, F.Cu at (126.0, 115.2)
- added D604: ES2A, Diode_SMD:D_MiniMELF_Handsoldering, F.Cu at (36.0, 115.2)
- added D605: ES2A, Diode_SMD:D_MiniMELF_Handsoldering, F.Cu at (234.5, 115.2)
- added D605: ES2A, Diode_SMD:D_MiniMELF_Handsoldering, F.Cu at (144.5, 115.2)
- added D605: ES2A, Diode_SMD:D_MiniMELF_Handsoldering, F.Cu at (54.5, 115.2)
- added D606: ES2A, Diode_SMD:D_MiniMELF_Handsoldering, B.Cu at (256.4, 156.7)
- added D606: ES2A, Diode_SMD:D_MiniMELF_Handsoldering, B.Cu at (166.4, 156.7)
- added D606: ES2A, Diode_SMD:D_MiniMELF_Handsoldering, B.Cu at (76.4, 156.7)
- added D607: LED_RED, LED_SMD:LED_0805_2012Metric_Pad1.15x1.40mm_HandSolder, F.Cu at (272.2, 99.1)
- added D607: LED_RED, LED_SMD:LED_0805_2012Metric_Pad1.15x1.40mm_HandSolder, F.Cu at (182.2, 99.1)
- added D607: LED_RED, LED_SMD:LED_0805_2012Metric_Pad1.15x1.40mm_HandSolder, F.Cu at (92.2, 99.1)
- added D608: LED_RED, LED_SMD:LED_0805_2012Metric_Pad1.15x1.40mm_HandSolder, F.Cu at (255.8, 175.2)
- added D608: LED_RED, LED_SMD:LED_0805_2012Metric_Pad1.15x1.40mm_HandSolder, F.Cu at (165.8, 175.2)
- added D608: LED_RED, LED_SMD:LED_0805_2012Metric_Pad1.15x1.40mm_HandSolder, F.Cu at (75.8, 175.2)
- added DZ601: 12V, Diode_SMD:D_MiniMELF_Handsoldering, F.Cu at (236.5, 132.5)
- added DZ601: 12V, Diode_SMD:D_MiniMELF_Handsoldering, F.Cu at (146.5, 132.5)
- added DZ601: 12V, Diode_SMD:D_MiniMELF_Handsoldering, F.Cu at (56.5, 132.5)
- added DZ602: 12V, Diode_SMD:D_MiniMELF_Handsoldering, F.Cu at (236.5, 129.5)
- added DZ602: 12V, Diode_SMD:D_MiniMELF_Handsoldering, F.Cu at (146.5, 129.5)
- added DZ602: 12V, Diode_SMD:D_MiniMELF_Handsoldering, F.Cu at (56.5, 129.5)
- added DZ603: 12V, Diode_SMD:D_MiniMELF_Handsoldering, F.Cu at (218.0, 132.5)
- added DZ603: 12V, Diode_SMD:D_MiniMELF_Handsoldering, F.Cu at (128.0, 132.5)
- added DZ603: 12V, Diode_SMD:D_MiniMELF_Handsoldering, F.Cu at (38.0, 132.5)
- added DZ604: 12V, Diode_SMD:D_MiniMELF_Handsoldering, F.Cu at (218.0, 129.5)
- added DZ604: 12V, Diode_SMD:D_MiniMELF_Handsoldering, F.Cu at (128.0, 129.5)
- added DZ604: 12V, Diode_SMD:D_MiniMELF_Handsoldering, F.Cu at (38.0, 129.5)
- added F501: 500mA, Fuse:Fuse_1206_3216Metric_Pad1.42x1.75mm_HandSolder, B.Cu at (210.8, 21.6)
- added F501: 500mA, Fuse:Fuse_1206_3216Metric_Pad1.42x1.75mm_HandSolder, B.Cu at (120.8, 21.6)
- added F501: 500mA, Fuse:Fuse_1206_3216Metric_Pad1.42x1.75mm_HandSolder, B.Cu at (30.9, 21.6)
- added F601: 10A, Fuse:Fuseholder_Cylinder-5x20mm_Stelvio-Kontek_PTF78_Horizontal_Open, B.Cu at (205.5, 151.3)
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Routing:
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- added copper zone on F.Cu, net Net-(F601-Pad2)
- added copper zone on B.Cu, net Net-(F602-Pad2)
- added copper zone on F.Cu, net Net-(F602-Pad2)
- removed copper zone on B.Cu, net +BATT
- removed copper zone on B.Cu, net Net-(C603-Pad1)
- removed copper zone on B.Cu, net Net-(F602-Pad1)
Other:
- board size 204 x 170.5 mm -> 261.5 x 172.8 mm
